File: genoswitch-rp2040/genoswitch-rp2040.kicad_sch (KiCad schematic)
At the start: 41 parts, among them J1 USB_B_Micro, J10 RP2040_ADC2, J11 RP2040_ADC3, J2 Conn_01x03_Socket-PicoDebug, J3 HW-SPI0, J4 HW-SPI1, J5 PIO-SPI0, J6 PIO-SPI1, J7 SERIAL, J8 RP2040_ADC0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

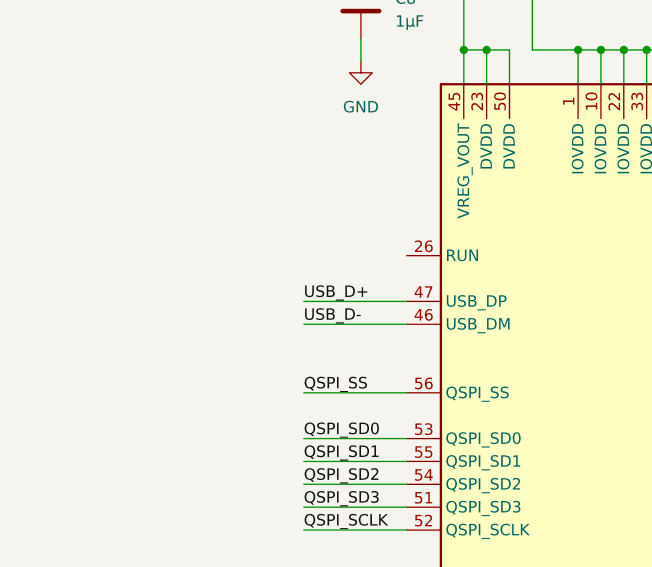
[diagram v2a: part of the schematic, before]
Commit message: (schematic): Add R6, R7 series termination resistors
TODO: document in schematic
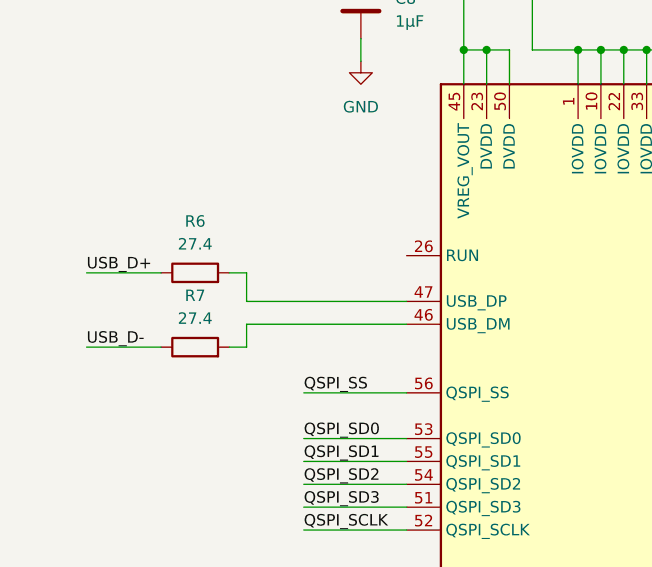
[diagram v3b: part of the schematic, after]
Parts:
- added R6, R7: 27.4, symbol Device:R
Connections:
- net USB_D+: now also R6.1; no longer U3.47 (USB_DP)
- net USB_D-: now also R7.1; no longer U3.46 (USB_DM)
- new net: R7.2, U3.46 (USB_DM)
- new net: R6.2, U3.47 (USB_DP)
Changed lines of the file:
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@@
+    (stroke (width 0) (type default))
+  )
+  (wire (pts (xy 20.32 78.74) (xy 28.575 78.74))
     (stroke (width 0) (type default))
   )
@@
     (stroke (width 0) (type default))
   )
+  (wire (pts (xy 38.1 76.2) (xy 55.88 76.2))
+    (stroke (width 0) (type default))
+  )
   (wire (pts (xy 227.33 84.455) (xy 228.6 84.455))
     (stroke (width 0) (type default))
@@
     (stroke (width 0) (type default))
   )
+  (wire (pts (xy 55.88 73.66) (xy 38.1 73.66))
+    (stroke (width 0) (type default))
+  )
   (wire (pts (xy 228.6 104.775) (xy 228.6 105.41))
     (stroke (width 0) (type default))
@@
     (stroke (width 0) (type default))
   )
+  (wire (pts (xy 38.1 73.66) (xy 38.1 70.485))
+    (stroke (width 0) (type default))
+  )
   (wire (pts (xy 233.68 147.32) (xy 233.68 148.59))
     (stroke (width 0) (type default))
@@
     (stroke (width 0) (type default))
   )
+  (wire (pts (xy 20.32 70.485) (xy 28.575 70.485))
+    (stroke (width 0) (type default))
+  )
   (wire (pts (xy 397.51 223.52) (xy 397.51 222.25))
     (stroke (width 0) (type default))
@@
     (stroke (width 0) (type default))
   )
+  (wire (pts (xy 36.195 78.74) (xy 38.1 78.74))
+    (stroke (width 0) (type default))
+  )
   (wire (pts (xy 190.5 101.6) (xy 192.786 101.6))
     (stroke (width 0) (type default))
@@
     (stroke (width 0) (type default))
   )
+  (wire (pts (xy 38.1 70.485) (xy 36.195 70.485))
+    (stroke (width 0) (type default))
+  )
   (wire (pts (xy 388.62 40.64) (xy 388.62 52.07))
     (stroke (width 0) (type default))
@@
     (stroke (width 0) (type default))
   )
+  (wire (pts (xy 38.1 78.74) (xy 38.1 76.2))
+    (stroke (width 0) (type default))
+  )
   (wire (pts (xy 55.88 91.44) (xy 44.45 91.44))
     (stroke (width 0) (type default))
   )
-  (wire (pts (xy 44.45 76.2) (xy 55.88 76.2))
-    (stroke (width 0) (type default))
-  )
   (wire (pts (xy 106.68 139.7) (xy 121.92 139.7))
     (stroke (width 0) (type default))
@@
   )
   (wire (pts (xy 106.68 83.82) (xy 121.92 83.82))
-    (stroke (width 0) (type default))
-  )
-  (wire (pts (xy 44.45 73.66) (xy 55.88 73.66))
     (stroke (width 0) (type default))
   )
@@
     (effects (font (size 1.27 1.27)) (justify left bottom))
   )
-  (label "USB_D+" (at 44.45 73.66 0) (fields_autoplaced)
+  (label "USB_D+" (at 20.32 70.485 0) (fields_autoplaced)
     (effects (font (size 1.27 1.27)) (justify left bottom))
   )
@@
     (effects (font (size 1.27 1.27)) (justify right bottom))
   )
-  (label "USB_D-" (at 44.45 76.2 0) (fields_autoplaced)
+  (label "USB_D-" (at 20.32 78.74 0) (fields_autoplaced)
     (effects (font (size 1.27 1.27)) (justify left bottom))
   )
@@
     )
   )
+  (symbol (lib_id "Device:R") (at 32.385 78.74 90) (unit 1)
+    (in_bom yes) (on_board yes) (dnp no) (fields_autoplaced)
+    (property "Reference" "R7" (at 32.385 73.025 90)
+      (effects (font (size 1.27 1.27)))
+    )
+    (property "Value" "27.4" (at 32.385 75.565 90)
+      (effects (font (size 1.27 1.27)))
+    )
+    (property "Footprint" "" (at 32.385 80.518 90)
+      (effects (font (size 1.27 1.27)) hide)
+    )
+    (property "Datasheet" "~" (at 32.385 78.74 0)
+      (effects (font (size 1.27 1.27)) hide)
+    )
+    (pin "1")
+    (pin "2")
+    (instances
+      (project "genoswitch-rp2040"
+        (path "/2e7ee4d9-1204-4a0f-bb2c-fb0f0d4af2cf"
+          (reference "R7") (unit 1)
+        )
+      )
+    )
+  )
   (symbol (lib_id "Connector:Conn_01x03_Socket") (at 336.55 139.7 0) (unit 1)
     (in_bom yes) (on_board yes) (dnp no)
@@
         )
       )
+    )
+  )
+  (symbol (lib_id "Device:R") (at 32.385 70.485 90) (unit 1)
+    (in_bom yes) (on_board yes) (dnp no) (fields_autoplaced)
+    (property "Reference" "R6" (at 32.385 64.77 90)
+      (effects (font (size 1.27 1.27)))
+    )
+    (property "Value" "27.4" (at 32.385 67.31 90)
+      (effects (font (size 1.27 1.27)))
+    )
+    (property "Footprint" "" (at 32.385 72.263 90)
+      (effects (font (size 1.27 1.27)) hide)
+    )
+    (property "Datasheet" "~" (at 32.385 70.485 0)
+      (effects (font (size 1.27 1.27)) hide)
+    )
+    (pin "1")
+    (pin "2")
+    (instances
+      (project "genoswitch-rp2040"
+        (path "/2e7ee4d9-1204-4a0f-bb2c-fb0f0d4af2cf"
+          (reference "R6") (unit 1)
+        )
+      )

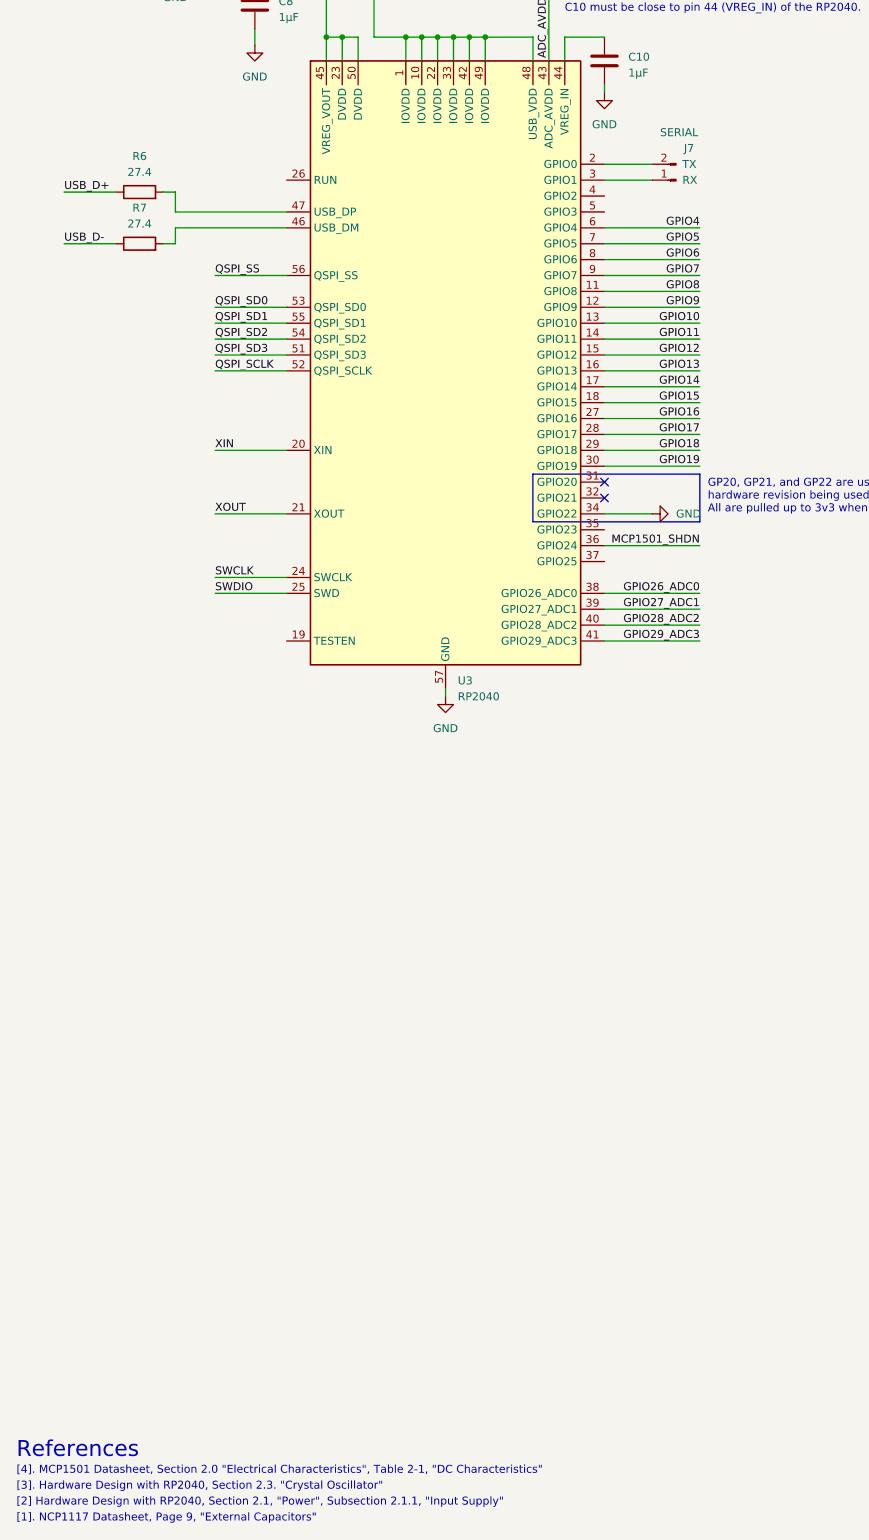
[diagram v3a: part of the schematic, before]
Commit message: Assign footprints, add notes to R6,R7
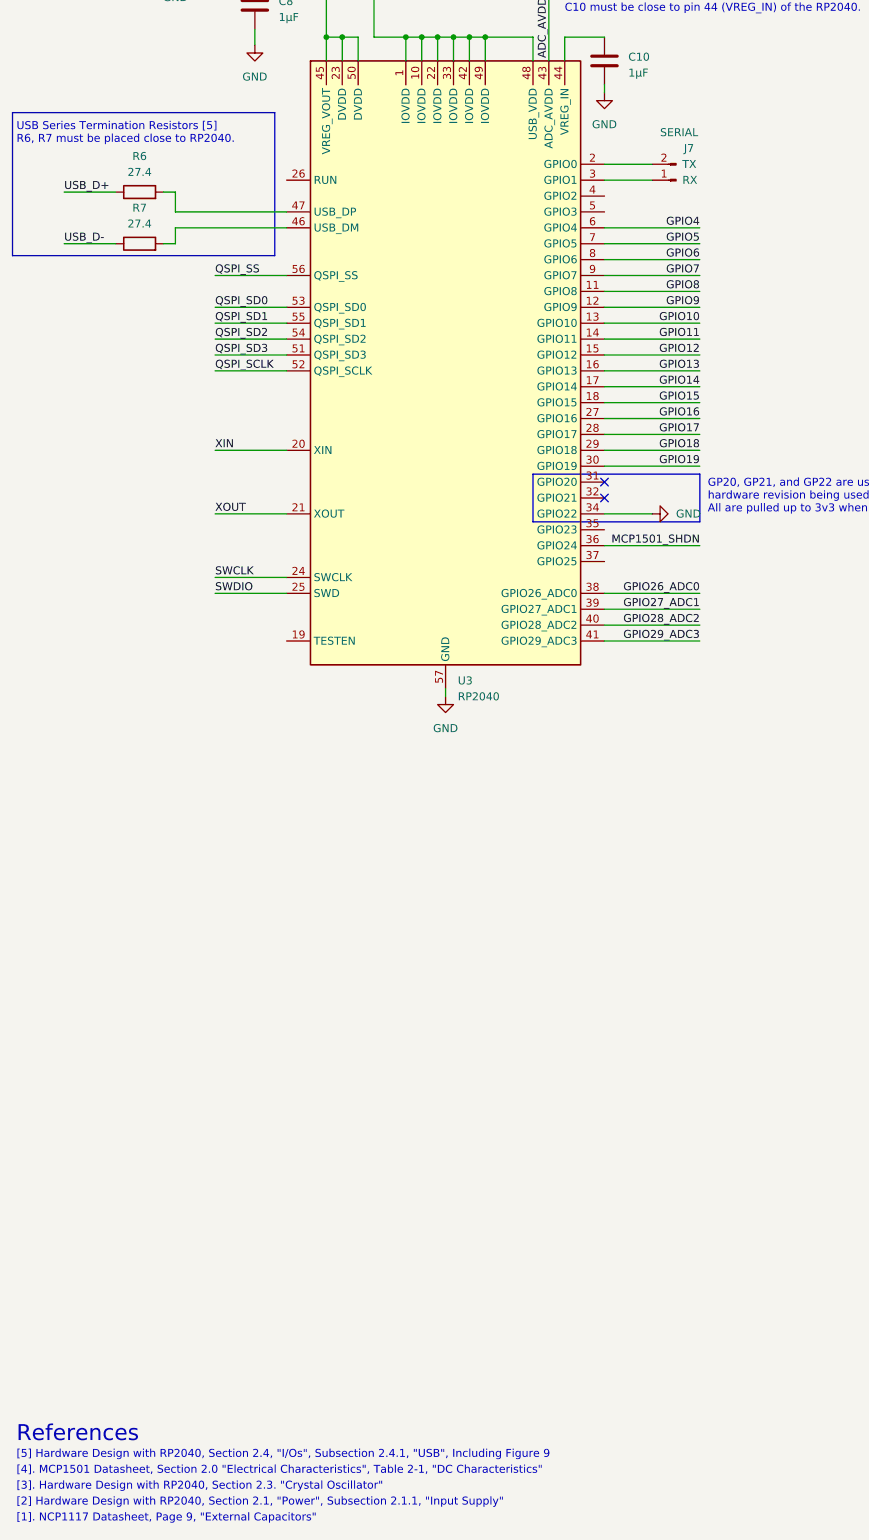
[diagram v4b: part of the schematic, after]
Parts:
- R6, R7: footprint (none) -> Resistor_SMD:R_0201_0603Metric
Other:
- note added: "USB Series Termination Resistors [5] R6, R7 must be placed close to RP2040."
- note added: "[5] Hardware Design with RP2040, Section 2.4, "I/Os", Subsection 2.4.1, "USB", Including Figure 9"
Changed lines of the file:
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@@
+    (fill (type none))
+  )
+  (rectangle (start 12.065 57.785) (end 53.975 80.645)
+    (stroke (width 0) (type default))
     (fill (type none))
   )
@@
     (effects (font (size 1.27 1.27)) (justify left bottom))
   )
+  (text "[5] Hardware Design with RP2040, Section 2.4, \"I/Os\", Subsection 2.4.1, \"USB\", Including Figure 9"
+    (at 12.7 273.05 0)
+    (effects (font (size 1.27 1.27)) (justify left bottom) (href "https://datasheets.raspberrypi.com/rp2040/hardware-design-with-rp2040.pdf"))
+  )
   (text "128Mbit (16MB) QSPI Flash" (at 378.46 15.24 0)
+    (effects (font (size 1.27 1.27)) (justify left bottom))
+  )
+  (text "USB Series Termination Resistors [5]\nR6, R7 must be placed close to RP2040."
+    (at 12.7 62.865 0)
     (effects (font (size 1.27 1.27)) (justify left bottom))
   )
@@
     (effects (font (size 1.27 1.27)) (justify left bottom) (href "https://datasheets.raspberrypi.com/rp2040/hardware-design-with-rp2040.pdf"))
   )
-  (text "References" (at 12.7 273.05 0)
+  (text "References" (at 12.7 270.51 0)
     (effects (font (size 2.54 2.54)) (justify left bottom))
   )
@@
       (effects (font (size 1.27 1.27)))
     )
-    (property "Footprint" "" (at 32.385 80.518 90)
+    (property "Footprint" "Resistor_SMD:R_0201_0603Metric" (at 32.385 80.518 90)
       (effects (font (size 1.27 1.27)) hide)
     )
@@
   )
   (symbol (lib_id "Device:R") (at 32.385 70.485 90) (unit 1)
-    (in_bom yes) (on_board yes) (dnp no) (fields_autoplaced)
+    (in_bom yes) (on_board yes) (dnp no)
     (property "Reference" "R6" (at 32.385 64.77 90)
       (effects (font (size 1.27 1.27)))
@@
       (effects (font (size 1.27 1.27)))
     )
-    (property "Footprint" "" (at 32.385 72.263 90)
-      (effects (font (size 1.27 1.27)) hide)
-    )
+    (property "Footprint" "Resistor_SMD:R_0201_0603Metric" (at 32.385 72.263 90)
+      (effects (font (size 1.27 1.27)) hide)
+    )

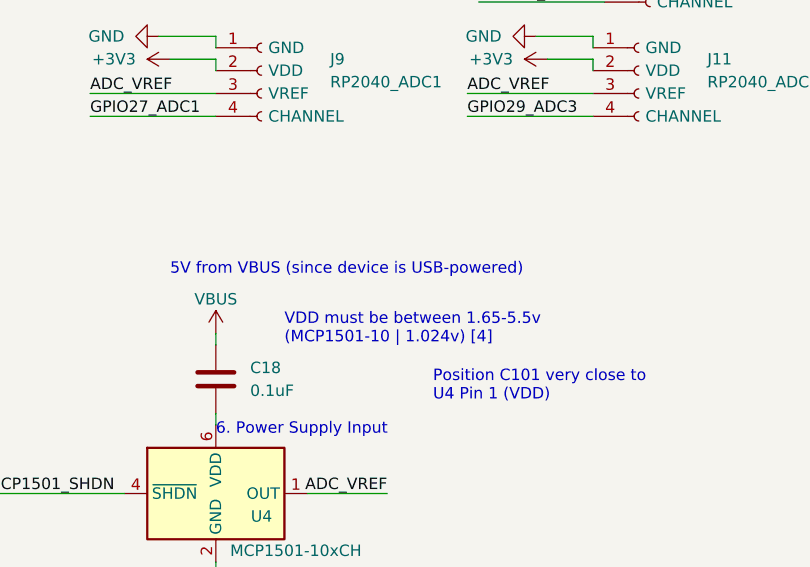
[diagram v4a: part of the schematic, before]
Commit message: Have U4 be powered by +3v3
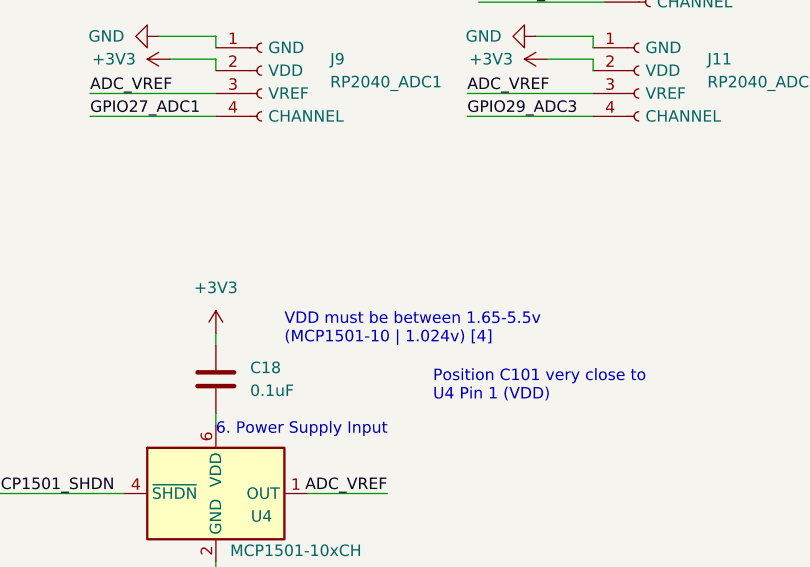
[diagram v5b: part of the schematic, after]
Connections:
- net +3V3: now also C18.2
- net VBUS: no longer C18.2
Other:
- note removed: "5V from VBUS (since device is USB-powered)"
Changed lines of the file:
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@@
     (effects (font (size 2.54 2.54)) (justify left bottom))
-  )
-  (text "5V from VBUS (since device is USB-powered)" (at 186.69 171.45 0)
-    (effects (font (size 1.27 1.27)) (justify left bottom))
   )
   (text "R1 is NOT required for\nthis PARTICULAR flash device."
@@
     )
   )
+  (symbol (lib_id "power:+3V3") (at 191.77 177.8 0) (unit 1)
+    (in_bom yes) (on_board yes) (dnp no) (fields_autoplaced)
+    (property "Reference" "#PWR019" (at 191.77 181.61 0)
+      (effects (font (size 1.27 1.27)) hide)
+    )
+    (property "Value" "+3V3" (at 191.77 172.72 0)
+      (effects (font (size 1.27 1.27)))
+    )
+    (property "Footprint" "" (at 191.77 177.8 0)
+      (effects (font (size 1.27 1.27)) hide)
+    )
+    (property "Datasheet" "" (at 191.77 177.8 0)
+      (effects (font (size 1.27 1.27)) hide)
+    )
+    (pin "1")
+    (instances
+      (project "genoswitch-rp2040"
+        (path "/2e7ee4d9-1204-4a0f-bb2c-fb0f0d4af2cf"
+          (reference "#PWR019") (unit 1)
+        )
+      )
+    )
+  )
   (symbol (lib_id "power:+3V3") (at 228.6 147.32 90) (unit 1)
     (in_bom yes) (on_board yes) (dnp no)
@@
         )
       )
-    )
-  )
-  (symbol (lib_id "power:VBUS") (at 191.77 177.8 0) (unit 1)
-    (in_bom yes) (on_board yes) (dnp no) (fields_autoplaced)
-    (property "Reference" "#PWR019" (at 191.77 181.61 0)
-      (effects (font (size 1.27 1.27)) hide)
-    )
-    (property "Value" "VBUS" (at 191.77 173.99 0)
-      (effects (font (size 1.27 1.27)))
-    )
-    (property "Footprint" "" (at 191.77 177.8 0)
-      (effects (font (size 1.27 1.27)) hide)
-    )
-    (property "Datasheet" "" (at 191.77 177.8 0)
-      (effects (font (size 1.27 1.27)) hide)
-    )
-    (pin "1")
-    (instances
-      (project "genoswitch-rp2040"
-        (path "/2e7ee4d9-1204-4a0f-bb2c-fb0f0d4af2cf"
-          (reference "#PWR019") (unit 1)
-        )
-      )

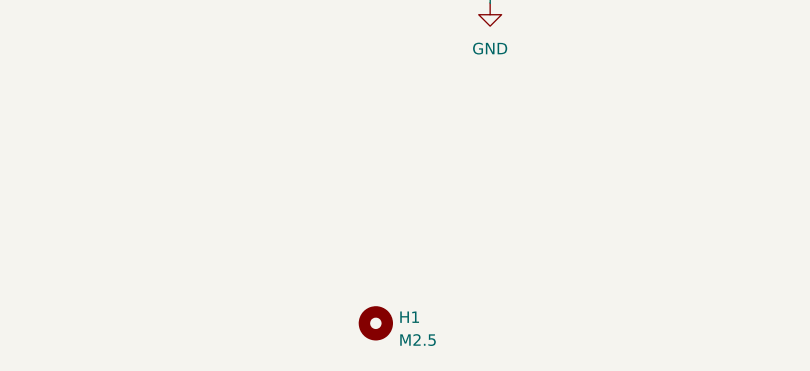
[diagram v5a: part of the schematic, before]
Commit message: (rp2040): Make screw hioles conductive on both layers
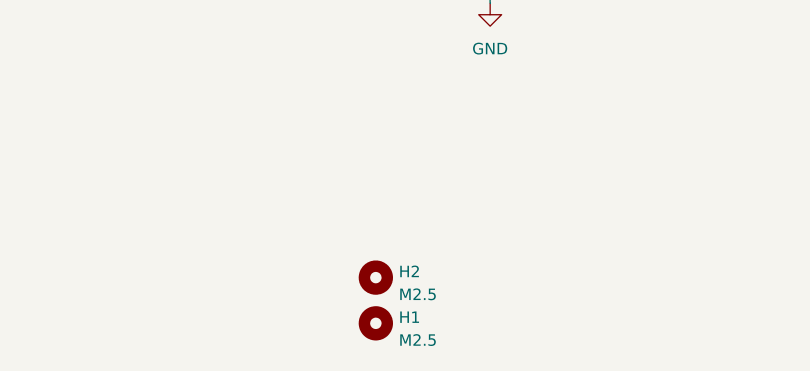
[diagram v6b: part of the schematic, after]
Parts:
- added H2: M2.5, MountingHole:MountingHole_2.7mm_M2.5_Pad_TopBottom, symbol Mechanical:MountingHole
- H1: footprint MountingHole:MountingHole_2.7mm_M2.5 -> MountingHole:MountingHole_2.7mm_M2.5_Pad_TopBottom
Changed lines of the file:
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@@
+    )
+  )
+  (symbol (lib_id "Mechanical:MountingHole") (at 290.83 275.59 0) (unit 1)
+    (in_bom yes) (on_board yes) (dnp no) (fields_autoplaced)
+    (property "Reference" "H2" (at 293.37 274.955 0)
+      (effects (font (size 1.27 1.27)) (justify left))
+    )
+    (property "Value" "M2.5" (at 293.37 277.495 0)
+      (effects (font (size 1.27 1.27)) (justify left))
+    )
+    (property "Footprint" "MountingHole:MountingHole_2.7mm_M2.5_Pad_TopBottom" (at 290.83 275.59 0)
+      (effects (font (size 1.27 1.27)) hide)
+    )
+    (property "Datasheet" "~" (at 290.83 275.59 0)
+      (effects (font (size 1.27 1.27)) hide)
+    )
+    (instances
+      (project "genoswitch-rp2040"
+        (path "/2e7ee4d9-1204-4a0f-bb2c-fb0f0d4af2cf"
+          (reference "H2") (unit 1)
+        )
+      )
     )
   )
@@
       (effects (font (size 1.27 1.27)) (justify left))
     )
-    (property "Footprint" "MountingHole:MountingHole_2.7mm_M2.5" (at 290.83 280.67 0)
-      (effects (font (size 1.27 1.27)) hide)
-    )
+    (property "Footprint" "MountingHole:MountingHole_2.7mm_M2.5_Pad_TopBottom" (at 290.83 280.67 0)
+      (effects (font (size 1.27 1.27)) hide)
+    )
